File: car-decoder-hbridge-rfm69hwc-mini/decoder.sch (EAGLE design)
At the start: 50 parts, among them U1 RFM69HCW, U2 ATMEGA328P-MU, U3 MCP73831, U6 MIC5219 3.3V, Y1 16MHZ

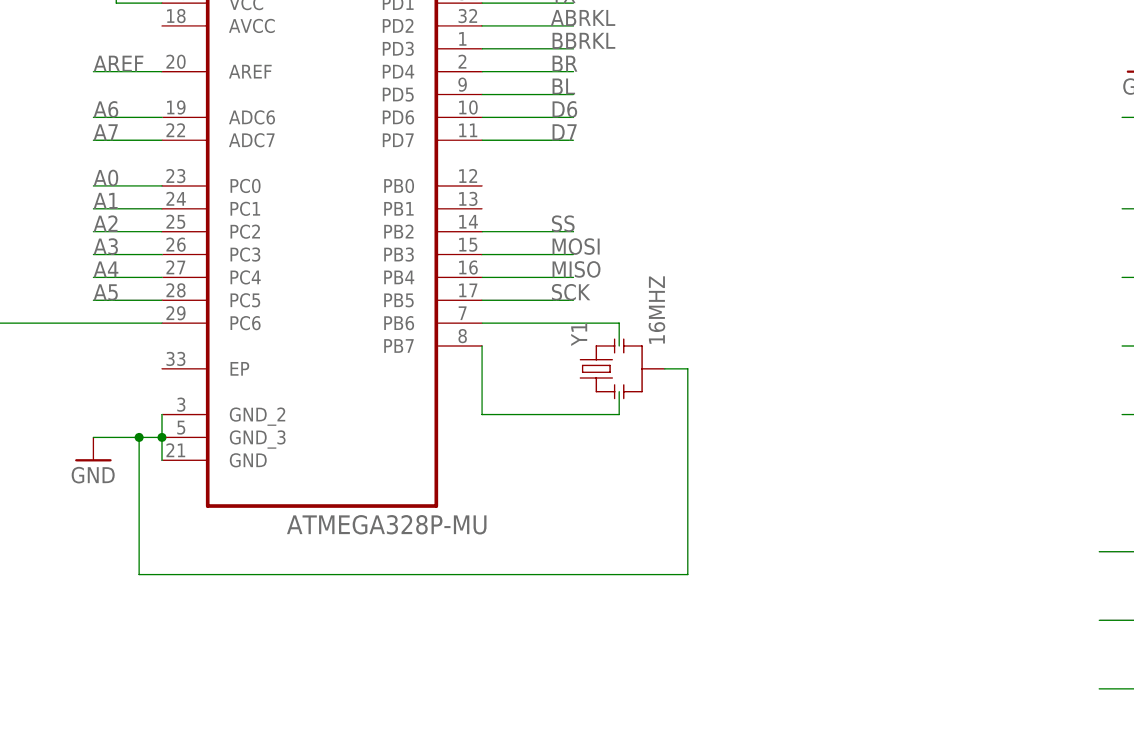
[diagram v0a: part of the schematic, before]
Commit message: Fix boards and add the pi control station
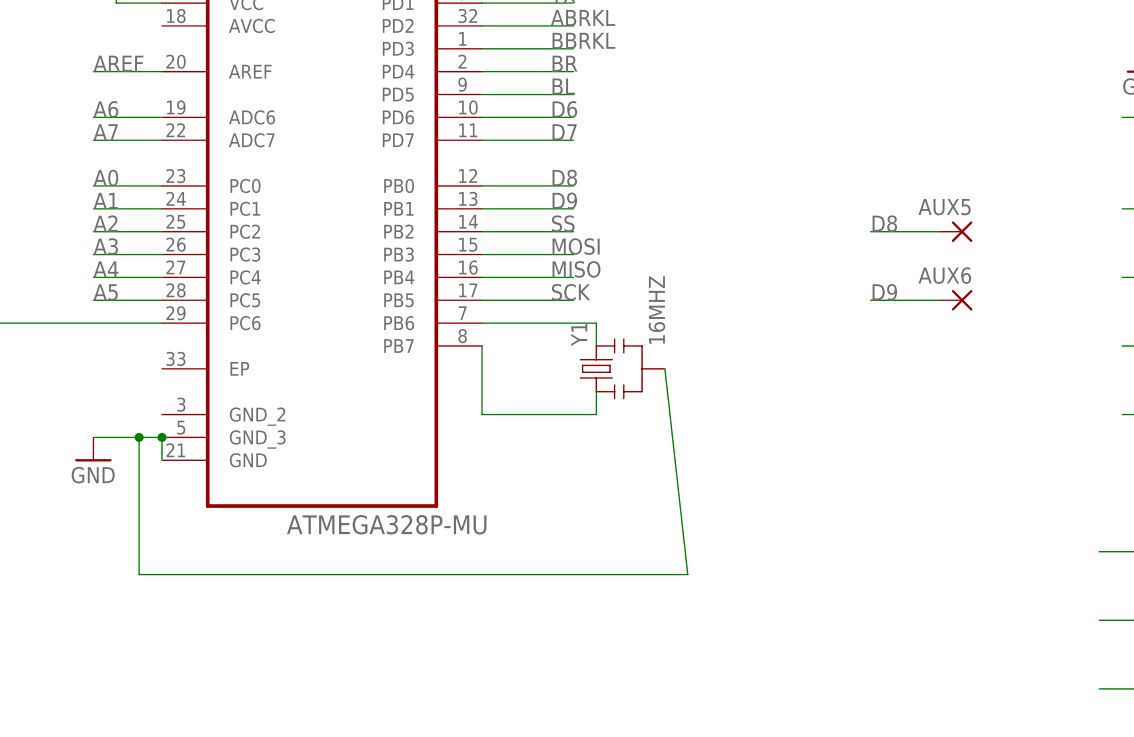
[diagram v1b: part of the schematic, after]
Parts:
- added AUX5, AUX6: (no value), wirepad:SMD2
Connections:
- new net D8: AUX5.P, U2.PB0
- new net D9: AUX6.P, U2.PB1
- net GND: no longer U2.GND_2
- net N$2: now also Y1.1
- net N$4: now also Y1.3
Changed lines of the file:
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@@
 <part name="SUPPLY2" library="SparkFun-Aesthetics" deviceset="VCC" device="" value="3.3V"/>
 <part name="U2" library="Atmel_By_element14_Batch_1-00" deviceset="ATMEGA328P-MU" device=""/>
+<part name="AUX5" library="wirepad" deviceset="SMD2" device=""/>
+<part name="AUX6" library="wirepad" deviceset="SMD2" device=""/>
 </parts>
 <sheets>
@@
 <instance part="SUPPLY2" gate="G$1" x="-15.24" y="43.18"/>
 <instance part="U2" gate="A" x="81.28" y="43.18"/>
+<instance part="AUX5" gate="1" x="152.4" y="38.1" rot="MR0"/>
+<instance part="AUX6" gate="1" x="152.4" y="30.48" rot="MR0"/>
 </instances>
 <busses>
@@
 </segment>
 <segment>
-<pinref part="U2" gate="A" pin="GND_2"/>
 <pinref part="U2" gate="A" pin="GND_3"/>
-<wire x1="63.5" y1="17.78" x2="63.5" y2="15.24" width="0.1524" layer="91"/>
 <pinref part="U2" gate="A" pin="GND"/>
 <wire x1="63.5" y1="12.7" x2="63.5" y2="15.24" width="0.1524" layer="91"/>
@@
 <junction x="60.96" y="15.24"/>
 <wire x1="60.96" y1="0" x2="121.92" y2="0" width="0.1524" layer="91"/>
-<wire x1="121.92" y1="0" x2="121.92" y2="22.86" width="0.1524" layer="91"/>
+<wire x1="121.92" y1="0" x2="119.38" y2="22.86" width="0.1524" layer="91"/>
 <pinref part="Y1" gate="G$1" pin="2"/>
-<wire x1="121.92" y1="22.86" x2="119.38" y2="22.86" width="0.1524" layer="91"/>
 </segment>
 </net>
@@
 <net name="N$2" class="0">
 <segment>
-<wire x1="114.3" y1="20.32" x2="114.3" y2="17.78" width="0.1524" layer="91"/>
+<wire x1="111.76" y1="20.32" x2="111.76" y2="17.78" width="0.1524" layer="91"/>
 <pinref part="U2" gate="A" pin="PB7"/>
-<wire x1="114.3" y1="17.78" x2="99.06" y2="17.78" width="0.1524" layer="91"/>
+<wire x1="111.76" y1="17.78" x2="99.06" y2="17.78" width="0.1524" layer="91"/>
 <wire x1="99.06" y1="17.78" x2="99.06" y2="25.4" width="0.1524" layer="91"/>
+<pinref part="Y1" gate="G$1" pin="1"/>
 </segment>
 </net>
 <net name="N$4" class="0">
 <segment>
-<wire x1="114.3" y1="25.4" x2="114.3" y2="27.94" width="0.1524" layer="91"/>
+<wire x1="111.76" y1="25.4" x2="111.76" y2="27.94" width="0.1524" layer="91"/>
 <pinref part="U2" gate="A" pin="PB6"/>
-<wire x1="114.3" y1="27.94" x2="99.06" y2="27.94" width="0.1524" layer="91"/>
+<wire x1="111.76" y1="27.94" x2="99.06" y2="27.94" width="0.1524" layer="91"/>
+<pinref part="Y1" gate="G$1" pin="3"/>
 </segment>
 </net>
@@
 </segment>
 </net>
+<net name="D8" class="0">
+<segment>
+<pinref part="U2" gate="A" pin="PB0"/>
+<wire x1="99.06" y1="43.18" x2="109.22" y2="43.18" width="0.1524" layer="91"/>
+<label x="106.68" y="43.18" size="1.778" layer="95"/>
+</segment>
+<segment>
+<pinref part="AUX5" gate="1" pin="P"/>
+<wire x1="149.86" y1="38.1" x2="142.24" y2="38.1" width="0.1524" layer="91"/>
+<label x="142.24" y="38.1" size="1.778" layer="95"/>
+</segment>
+</net>
+<net name="D9" class="0">
+<segment>
+<pinref part="U2" gate="A" pin="PB1"/>
+<wire x1="99.06" y1="40.64" x2="109.22" y2="40.64" width="0.1524" layer="91"/>
+<label x="106.68" y="40.64" size="1.778" layer="95"/>
+</segment>
+<segment>
+<pinref part="AUX6" gate="1" pin="P"/>
+<wire x1="149.86" y1="30.48" x2="142.24" y2="30.48" width="0.1524" layer="91"/>
+<label x="142.24" y="30.48" size="1.778" layer="95"/>
+</segment>
+</net>
